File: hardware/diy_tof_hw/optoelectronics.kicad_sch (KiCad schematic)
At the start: 39 parts, among them IC21 74LVC1G08QW5-7, IC22 LMG1025QDEETQ1, SW2 SW_Nidec_CAS-120A1, U2 OPA858xDSG, U3 TLV3501AIDBV

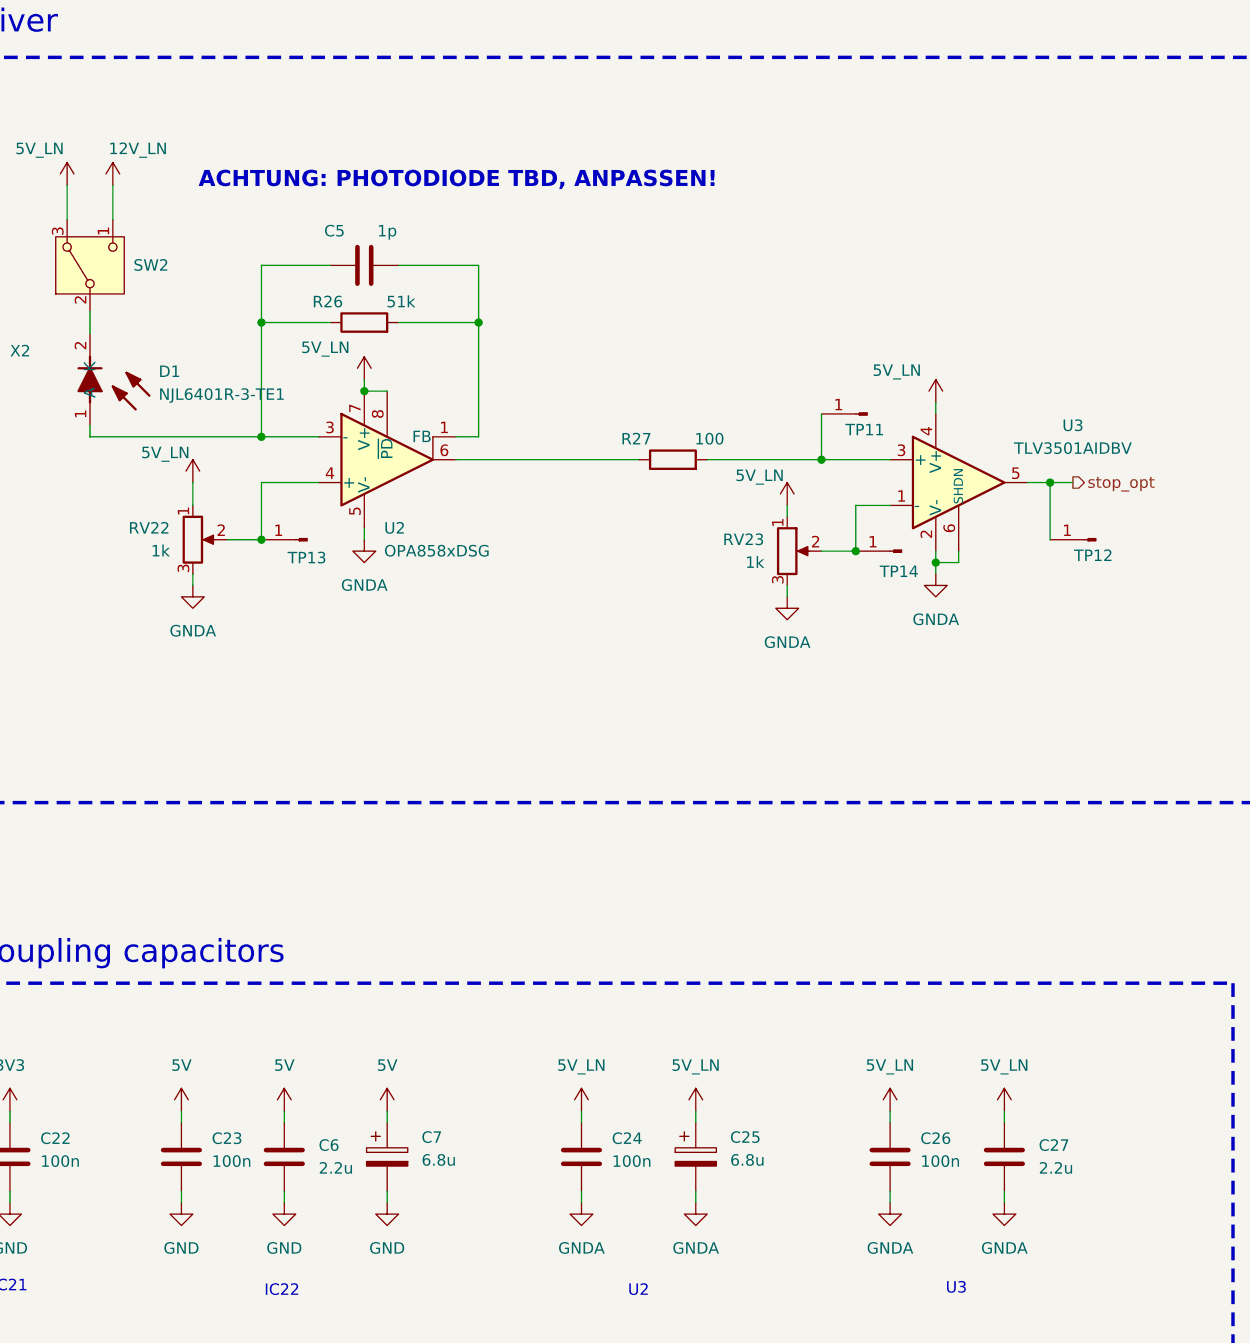
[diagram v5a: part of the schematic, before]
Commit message: [hardware] added mounting holes, reannotated some caps, started placement of the TIA part
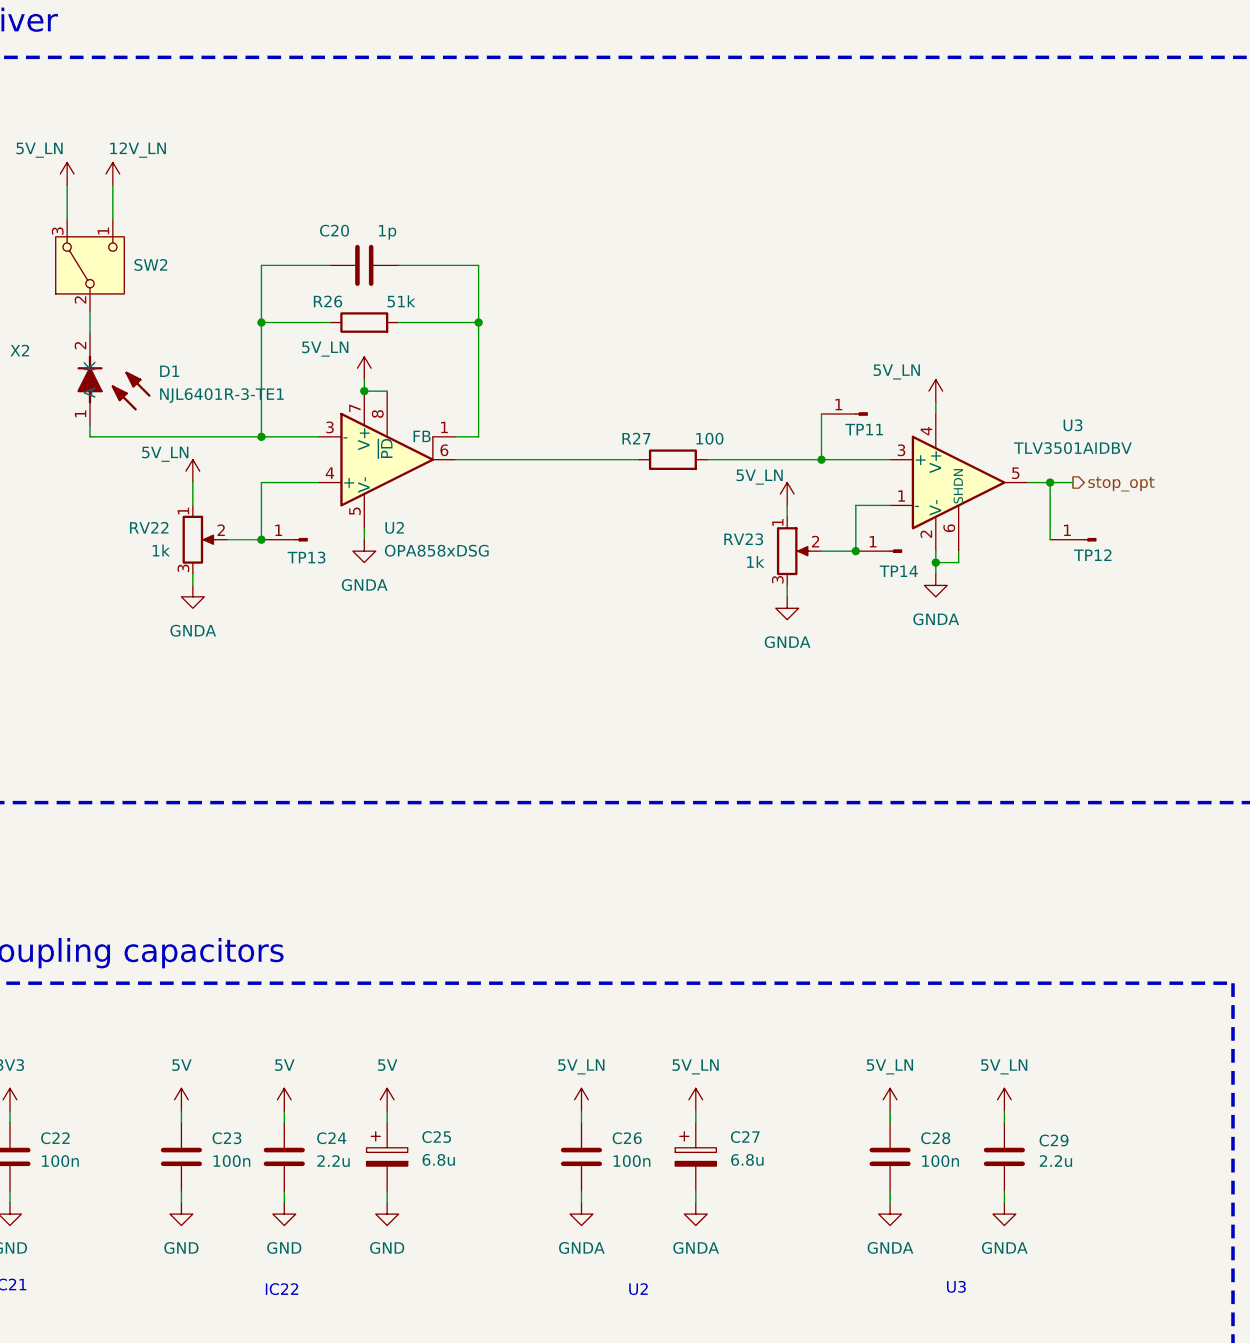
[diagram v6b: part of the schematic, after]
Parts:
- renumbered C5 to C20, C6 to C24, C7 to C25, C24 to C26, C25 to C27, C26 to C28, C27 to C29
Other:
- note removed: "ACHTUNG: PHOTODIODE TBD, ANPASSEN!"
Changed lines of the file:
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@@
 		)
 	)
-	(text "ACHTUNG: PHOTODIODE TBD, ANPASSEN!"
-		(exclude_from_sim no)
-		(at 106.934 130.302 0)
-		(effects
-			(font
-				(size 1.778 1.778)
-				(thickness 0.3556)
-				(bold yes)
-				(color 255 36 34 1)
-			)
-		)
-	)
 	(text "Tp equals ~tau \n     -> 0.5 ... 100 ns"
 		(exclude_from_sim no)
@@
 		(on_board yes)
 		(dnp no)
-		(property "Reference" "C24"
+		(property "Reference" "C26"
 			(at 125.73 236.728 0)
 			(effects
@@
 			(project "diy_tof_hw"
 				(path "/0f7bf370-0a80-4101-a61d-d850fd66ab1d/1536e9f2-3315-42ae-af66-5ae730c43aea"
-					(reference "C24")
+					(reference "C26")
 					(unit 1)
 				)
@@
 		(on_board yes)
 		(dnp no)
-		(property "Reference" "C26"
+		(property "Reference" "C28"
 			(at 160.02 236.728 0)
 			(effects
@@
 			(project "diy_tof_hw"
 				(path "/0f7bf370-0a80-4101-a61d-d850fd66ab1d/1536e9f2-3315-42ae-af66-5ae730c43aea"
-					(reference "C26")
+					(reference "C28")
 					(unit 1)
 				)
@@
 		(on_board yes)
 		(dnp no)
-		(property "Reference" "C5"
+		(property "Reference" "C20"
 			(at 93.218 135.89 90)
 			(effects
@@
 			(project "diy_tof_hw"
 				(path "/0f7bf370-0a80-4101-a61d-d850fd66ab1d/1536e9f2-3315-42ae-af66-5ae730c43aea"
-					(reference "C5")
+					(reference "C20")
 					(unit 1)
 				)
@@
 		(dnp no)
 		(fields_autoplaced yes)
-		(property "Reference" "C7"
+		(property "Reference" "C25"
 			(at 102.87 236.6009 0)
 			(effects
@@
 			(project "diy_tof_hw"
 				(path "/0f7bf370-0a80-4101-a61d-d850fd66ab1d/1536e9f2-3315-42ae-af66-5ae730c43aea"
-					(reference "C7")
+					(reference "C25")
 					(unit 1)
 				)
@@
 		(on_board yes)
 		(dnp no)
-		(fields_autoplaced yes)
-		(property "Reference" "C27"
-			(at 171.45 237.4899 0)
+		(property "Reference" "C29"
+			(at 171.45 236.982 0)
 			(effects
 				(font
@@
 		)
 		(property "Value" "2.2u"
-			(at 171.45 240.0299 0)
+			(at 171.45 239.268 0)
 			(effects
 				(font
@@
 			(project ""
 				(path "/0f7bf370-0a80-4101-a61d-d850fd66ab1d/1536e9f2-3315-42ae-af66-5ae730c43aea"
-					(reference "C27")
+					(reference "C29")
 					(unit 1)
 				)
@@
 		(on_board yes)
 		(dnp no)
-		(fields_autoplaced yes)
-		(property "Reference" "C6"
-			(at 91.44 237.4899 0)
+		(property "Reference" "C24"
+			(at 91.186 236.728 0)
 			(effects
 				(font
@@
 		)
 		(property "Value" "2.2u"
-			(at 91.44 240.0299 0)
+			(at 91.186 239.268 0)
 			(effects
 				(font
@@
 			(project "diy_tof_hw"
 				(path "/0f7bf370-0a80-4101-a61d-d850fd66ab1d/1536e9f2-3315-42ae-af66-5ae730c43aea"
-					(reference "C6")
+					(reference "C24")
 					(unit 1)
 				)
@@
 		(dnp no)
 		(fields_autoplaced yes)
-		(property "Reference" "C25"
+		(property "Reference" "C27"
 			(at 137.16 236.6009 0)
 			(effects
@@
 			(project ""
 				(path "/0f7bf370-0a80-4101-a61d-d850fd66ab1d/1536e9f2-3315-42ae-af66-5ae730c43aea"
-					(reference "C25")
+					(reference "C27")
 					(unit 1)
 				)
